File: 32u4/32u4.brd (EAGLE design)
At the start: 35.6 x 29.8 mm, 16 parts, among them J1 AVR_SPI_PRG_62X3_LOCK

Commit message: Latest controller revision
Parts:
- removed LED1: (no value), SparkFun-LED:LED-1206
- removed R5: (no value), SparkFun-Resistors:0805
- added C4: 1uF, SparkFun-Capacitors:0805
- added C5, C6: 100uF, resistor:C1608
- added JP2: (no value), pinhead:2X07
- added R6, R7: 150, SparkFun-Resistors:0805
- added R8: 330, SparkFun-Resistors:0805
- added S1: SWITCH-MOMENTARY-2SMD-3, SparkFun-Electromechanical:TACTILE_SWITCH_SMD-3
- added U$5: LED-RGB, IntegerLabs:LED-LITEON-SMD-RGB
- added U$6: TACT-SWITCHBOURNS-7914J, IntegerLabs:BOURNS-7914J
- C2, C3: value (none) -> 18pF
- D1: value (none) -> b340b; device adafruit:SMADIODE -> SparkFun-DiscreteSemi:SMB-DIODE
- J1: value AVR_SPI_PRG_62X3_LOCK -> AVR_SPI_PRG_6PTH; device SparkFun-Connectors:2X3_LOCK -> SparkFun-Connectors:2X3
- R1, R2: value (none) -> 2k
- U$4: value USB-MICRO-AB -> USBFCI-MICROB; device IntegerLabs:MOLEX-MICROAB -> IntegerLabs:USB-MICROB-FCI
- moved U$1 20.1 mm to (27.0, 3.17), turned to 180 degrees
- moved R2 12.3 mm to (5.08, 8.26), turned to 0 degrees
- moved U$4 11.4 mm to (10.2, 1.45)
- moved D1 8.47 mm to (19.1, 3.17), turned to 180 degrees
- moved R4 7.84 mm to (7.94, 7.30), turned to 90 degrees
- moved C2 7.81 mm to (23.2, 17.8), turned to 90 degrees
- moved R3 5.02 mm to (9.84, 7.30), turned to 90 degrees
- moved Y1 4.80 mm to (20.3, 16.2)
- moved C3 4.32 mm to (23.2, 14.6), turned to 270 degrees
- moved C1 4.24 mm to (11.7, 7.30), turned to 270 degrees
- moved J1 2.96 mm to (23.2, 10.2), turned to 180 degrees
- moved R1 2.29 mm to (5.08, 10.2), turned to 0 degrees
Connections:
- removed net LED: R5.2, U$2.32
- removed net N$3: LED1.A, R5.1
- new net A0: JP2.7, U$2.36
- new net A1: JP2.8, U$2.37
- new net A2: JP2.5, U$2.38
- new net A3: JP2.6, U$2.39
- new net A4: JP2.3, U$2.40
- new net A5: JP2.4, U$2.41
- new net B: R6.1, U$2.32
- new net D5: JP2.10, U$2.31
- new net D6: JP2.12, U$2.27
- new net D8: JP2.14, U$2.28
- new net D9: JP2.13, U$2.29
- new net G: R7.1, U$2.12
- new net N$10: R6.2, U$5.1
- new net N$6: R8.2, U$5.2
- new net N$7: R7.2, U$5.3
- new net R: R8.1, U$2.30
- new net SWITCH: U$2.20, U$6.POS$1
- net D+: now also U$4.P3; no longer U$4.3
- net D-: now also U$4.P2; no longer U$4.2
- net GND: now also C4.2, C5.2, C6.2, JP2.1, S1.1, U$3.BUS0, U$4.P5, U$6.NEG$1; no longer LED1.C, U$3.GND, U$4.5
- net MISO: no longer U$3.MISO
- net RESET: now also S1.4; no longer U$3.RESET
- net SCL: now also JP2.11, U$3.BUS3; no longer U$3.SCL
- net SDA: now also JP2.9, U$3.BUS1; no longer U$3.SDA
- net VBUS: now also U$4.P1; no longer U$4.1
- net VCC: now also C4.1, C5.1, C6.1, JP2.2, U$3.BUS2, U$5.4; no longer U$3.VCC
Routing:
- net GND: track 23.4 -> 132.2 mm, vias 9 -> 7
- net VCC: track 63.4 -> 97.1 mm, vias 2 -> 3
- net SCL: track 15.8 -> 48.2 mm, vias 2 -> 5
- net G: track 0.00 -> 31.4 mm
- net A4: track 0.00 -> 29.8 mm, vias 0 -> 1
- net A2: track 0.00 -> 29.2 mm, vias 0 -> 1
- net A0: track 0.00 -> 29.0 mm, vias 0 -> 1
- net MISO: track 39.7 -> 11.1 mm, vias 2 -> 1
- net A3: track 0.00 -> 28.2 mm, vias 0 -> 2
- net A5: track 0.00 -> 26.8 mm, vias 0 -> 1
- net A1: track 0.00 -> 26.0 mm, vias 0 -> 1
- net D5: track 0.00 -> 25.8 mm, vias 0 -> 1
- net D8: track 0.00 -> 24.0 mm, vias 0 -> 1
- net D9: track 0.00 -> 23.3 mm, vias 0 -> 1
- net D6: track 0.00 -> 23.1 mm, vias 0 -> 1
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- removed copper zone on layer 16, net GND
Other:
- outline, holes or cut-outs redrawn
- board text added: "+"
- board text added: "-"
- board text added: "2014-09-14"
- board text added: "A0"
- board text added: "A1"
- board text added: "A2"
- board text added: "A3"
- board text added: "A4"
- board text added: "A5"
- board text added: "Controller"
- board text added: "D5"
- board text added: "D6"
- board text added: "D8"
- board text added: "D9"
- board text added: "Integer Labs"
- board text added: "Modulo"
- board text added: "icsp"
- board text added: "reset"
- board text added: "scl"
- board text added: "sda"

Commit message: Latest version of schematics and boards
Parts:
- removed C5: 100uF, resistor:C1608
- added F2: .5A, IntegerLabs:1812
- added Q1, Q3: IRLML5203, transistor-power:MICRO3
- added Q2: DMMT5401, IntegerLabs:SOT-26
- added R5, R9: 47k 1%, SparkFun-Passives:0805
- F1: value FUSE -> 1.5A
- renumbered U$1 to F1
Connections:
- new net N$11: F2.P$2, Q1.3, Q2.6, Q3.3
- new net N$13: Q2.5, Q3.2
- new net N$14: Q2.1, Q2.2, Q2.3, R5.2
- new net N$16: Q2.4, Q3.1, R9.2
- new net N$3: F1.P$1, F2.P$1, U$4.P1
- net GND: now also R5.1, R9.1; no longer C5.2
- net N$5: now also Q1.2; no longer D1.C
- net VBUS: no longer U$4.P1
- net VCC: no longer C5.1, C6.1, F1.P$1
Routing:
- net VCC: track 97.1 -> 91.4 mm
- net N$5: track 3.20 -> 0.00 mm
- net GND: track 132.2 -> 129.0 mm
- net VBUS: track 28.6 -> 27.0 mm
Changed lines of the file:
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@@
 <attribute name="VALUE" x="4.953" y="7.112" size="0.4064" layer="27" ratio="10"/>
 </element>
-<element name="U$1" library="IntegerLabs" package="1812" value="FUSE" x="26.9875" y="3.175" rot="R180"/>
+<element name="F1" library="IntegerLabs" package="1812" value="1.5A" x="26.9875" y="3.175" rot="R180"/>
 <element name="S1" library="SparkFun-Electromechanical" package="TACTILE_SWITCH_SMD-3" value="SWITCH-MOMENTARY-2SMD-3" x="23.0505" y="27.3685" rot="R180"/>
 <element name="JP2" library="pinhead" package="2X07" value="" x="29.21" y="13.97" smashed="yes" rot="R90">
@@
 <attribute name="NAME" x="6.5405" y="12.2555" size="0.4064" layer="25" ratio="10"/>
 <attribute name="VALUE" x="6.604" y="11.6205" size="0.4064" layer="27" ratio="10"/>
-</element>
-<element name="C5" library="resistor" package="C1608" value="100uF" x="14.605" y="10.16" smashed="yes" rot="R180">
-<attribute name="NAME" x="15.367" y="9.398" size="0.508" layer="25" rot="R180"/>
-<attribute name="VALUE" x="15.875" y="11.43" size="0.508" layer="27" rot="R180"/>
 </element>
 <element name="C6" library="resistor" package="C1608" value="100uF" x="14.605" y="6.985" smashed="yes" rot="R180">
@@
 </element>
 <element name="U$6" library="IntegerLabs" package="BOURNS-7914J" value="TACT-SWITCHBOURNS-7914J" x="20.955" y="21.9075" rot="R90"/>
+<element name="Q1" library="transistor-power" package="MICRO3" value="IRLML5203" x="1.27" y="-5.08"/>
+<element name="F2" library="IntegerLabs" package="1812" value=".5A" x="2.54" y="-11.43"/>
+<element name="Q2" library="IntegerLabs" package="SOT-26" value="DMMT5401" x="-3.81" y="-11.43"/>
+<element name="R5" library="SparkFun-Passives" package="0805" value="47k 1%" x="-7.62" y="-11.43"/>
+<element name="R9" library="SparkFun-Passives" package="0805" value="47k 1%" x="-11.43" y="-11.43"/>
+<element name="Q3" library="transistor-power" package="MICRO3" value="IRLML5203" x="-10.16" y="-17.78"/>
 </elements>
 <signals>
@@
 <contactref element="S1" pad="1"/>
 <contactref element="C4" pad="2"/>
-<contactref element="C5" pad="2"/>
 <contactref element="C6" pad="2"/>
 <wire x1="5.98" y1="12.065" x2="5.98" y2="13.07" width="0.254" layer="1"/>
@@
 <wire x1="3.4925" y1="11.43" x2="5.08" y2="11.43" width="0.508" layer="16"/>
 <wire x1="5.08" y1="11.43" x2="5.08" y2="13.97" width="0.1524" layer="16"/>
-<wire x1="13.755" y1="10.16" x2="13.755" y2="6.985" width="0.508" layer="1"/>
 <wire x1="13.755" y1="6.985" x2="13.755" y2="5.6125" width="0.508" layer="1"/>
 <wire x1="13.755" y1="5.6125" x2="13.97" y2="5.3975" width="0.508" layer="1"/>
+<contactref element="R5" pad="1"/>
+<contactref element="R9" pad="1"/>
+<wire x1="-8.52" y1="-11.43" x2="-12.33" y2="-11.43" width="0" layer="19" extent="1-1"/>
+<wire x1="3.4925" y1="5.3975" x2="-8.52" y2="-11.43" width="0" layer="19" extent="1-16"/>
 </signal>
 <signal name="VCC">
@@
 <contactref element="R2" pad="1"/>
 <contactref element="R1" pad="1"/>
-<contactref element="U$1" pad="P$1"/>
 <wire x1="7.595" y1="13.885" x2="7.595" y2="15.265" width="0.1524" layer="1"/>
 <wire x1="7.595" y1="15.265" x2="6.985" y2="15.875" width="0.1524" layer="1"/>
@@
 <contactref element="JP2" pad="2"/>
 <contactref element="C4" pad="1"/>
-<contactref element="C5" pad="1"/>
-<contactref element="C6" pad="1"/>
 <wire x1="4.18" y1="12.065" x2="4.18" y2="12.0125" width="0.254" layer="1"/>
 <wire x1="4.18" y1="12.0125" x2="5.08" y2="11.1125" width="0.254" layer="1"/>
@@
 <wire x1="4.18" y1="10.16" x2="4.18" y2="10.2125" width="0.254" layer="1"/>
 <wire x1="4.18" y1="10.2125" x2="5.08" y2="11.1125" width="0.254" layer="1"/>
-<wire x1="29.5275" y1="3.175" x2="28.575" y2="3.175" width="0.254" layer="1"/>
 <wire x1="28.575" y1="3.175" x2="27.94" y2="3.81" width="0.254" layer="1"/>
 <wire x1="27.94" y1="3.81" x2="27.94" y2="6.35" width="0.254" layer="1"/>
@@
 <wire x1="16.1925" y1="5.3975" x2="15.5575" y2="6.0325" width="0.254" layer="1"/>
 <wire x1="15.5575" y1="6.0325" x2="15.5575" y2="6.8825" width="0.254" layer="1"/>
-<wire x1="15.5575" y1="6.8825" x2="15.455" y2="6.985" width="0.254" layer="1"/>
 <contactref element="J1" pad="2"/>
 <wire x1="4.995" y1="23.685" x2="3.0475" y2="23.685" width="0.1524" layer="1"/>
@@
 <wire x1="14.605" y1="15.5575" x2="14.605" y2="17.145" width="0.1524" layer="1"/>
 <wire x1="14.2875" y1="26.9875" x2="13.97" y2="26.67" width="0.1524" layer="1"/>
-<wire x1="15.455" y1="6.985" x2="15.455" y2="10.16" width="0.508" layer="1"/>
-<wire x1="15.455" y1="10.16" x2="15.455" y2="11.5325" width="0.508" layer="1"/>
 <wire x1="15.455" y1="11.5325" x2="15.24" y2="11.7475" width="0.508" layer="1"/>
 <wire x1="15.24" y1="11.7475" x2="11.7475" y2="11.7475" width="0.508" layer="1"/>
@@
 <wire x1="9.525" y1="9.2075" x2="10.16" y2="9.8425" width="0.1524" layer="16"/>
 <wire x1="10.16" y1="9.8425" x2="10.16" y2="11.43" width="0.1524" layer="16"/>
+<wire x1="15.455" y1="11.5325" x2="15.5575" y2="6.8825" width="0" layer="19" extent="1-1"/>
 </signal>
 <signal name="D-">
@@
 <signal name="VBUS">
 <contactref element="U$2" pad="7"/>
-<contactref element="U$4" pad="P1"/>
 <contactref element="D1" pad="A"/>
-<wire x1="8.86" y1="4.1478" x2="8.86" y2="3.205" width="0.254" layer="1"/>
 <wire x1="8.86" y1="3.205" x2="9.2075" y2="2.8575" width="0.254" layer="1"/>
-<wire x1="8.86" y1="4.1478" x2="8.86" y2="4.7925" width="0.254" layer="1"/>
 <wire x1="8.86" y1="4.7925" x2="8.255" y2="5.3975" width="0.254" layer="1"/>
 <wire x1="8.255" y1="5.3975" x2="6.985" y2="5.3975" width="0.254" layer="1"/>
@@
 <wire x1="11.43" y1="12.7" x2="11.43" y2="13.72" width="0.254" layer="1"/>
 <wire x1="11.43" y1="13.72" x2="11.595" y2="13.885" width="0.254" layer="1"/>
+<wire x1="8.86" y1="3.205" x2="8.86" y2="4.7925" width="0" layer="19" extent="1-1"/>
 </signal>
 <signal name="RESET">
@@
 <wire x1="20.9575" y1="13.705" x2="20.32" y2="14.3425" width="0.1524" layer="1"/>
 </signal>
-<signal name="N$5">
-<contactref element="D1" pad="C"/>
-<contactref element="U$1" pad="P$2"/>
-<wire x1="21.25" y1="3.175" x2="24.4475" y2="3.175" width="0.254" layer="1"/>
-</signal>
 <signal name="A0">
 <contactref element="U$2" pad="36"/>
@@
 <wire x1="10.4775" y1="23.1775" x2="8.89" y2="23.1775" width="0.2032" layer="1"/>
 </signal>
+<signal name="N$3">
+<contactref element="U$4" pad="P1"/>
+<contactref element="F2" pad="P$1"/>
+<contactref element="F1" pad="P$1"/>
+<wire x1="8.86" y1="4.1478" x2="29.5275" y2="3.175" width="0" layer="19" extent="1-1"/>
+<wire x1="0" y1="-11.43" x2="8.86" y2="4.1478" width="0" layer="19" extent="1-1"/>
+</signal>
+<signal name="N$5">
+<contactref element="Q1" pad="2"/>
+<contactref element="F1" pad="P$2"/>
+<wire x1="2.22" y1="-6.08" x2="24.4475" y2="3.175" width="0" layer="19" extent="1-1"/>
+</signal>
+<signal name="N$11">
+<contactref element="Q1" pad="3"/>
+<contactref element="F2" pad="P$2"/>
+<contactref element="Q2" pad="6"/>
+<contactref element="Q3" pad="3"/>
+<wire x1="-4.76" y1="-10.23" x2="-10.16" y2="-16.78" width="0" layer="19" extent="1-1"/>
+<wire x1="1.27" y1="-4.08" x2="-4.76" y2="-10.23" width="0" layer="19" extent="1-1"/>
+<wire x1="5.08" y1="-11.43" x2="1.27" y2="-4.08" width="0" layer="19" extent="1-1"/>
+</signal>
+<signal name="N$13">
+<contactref element="Q2" pad="5"/>
+<contactref element="Q3" pad="2"/>
+<wire x1="-3.81" y1="-10.23" x2="-9.21" y2="-18.78" width="0" layer="19" extent="1-1"/>
+</signal>
+<signal name="N$14">
+<contactref element="Q2" pad="2"/>
+<contactref element="Q2" pad="1"/>
+<contactref element="Q2" pad="3"/>
+<contactref element="R5" pad="2"/>
+<wire x1="-4.76" y1="-12.63" x2="-6.72" y2="-11.43" width="0" layer="19" extent="1-1"/>
+<wire x1="-3.81" y1="-12.63" x2="-4.76" y2="-12.63" width="0" layer="19" extent="1-1"/>
+<wire x1="-2.86" y1="-12.63" x2="-3.81" y2="-12.63" width="0" layer="19" extent="1-1"/>
+</signal>
+<signal name="N$16">
+<contactref element="Q2" pad="4"/>
+<contactref element="R9" pad="2"/>
+<contactref element="Q3" pad="1"/>
+<wire x1="-10.53" y1="-11.43" x2="-11.11" y2="-18.78" width="0" layer="19" extent="1-1"/>
+<wire x1="-2.86" y1="-10.23" x2="-10.53" y2="-11.43" width="0" layer="19" extent="1-1"/>
+</signal>
 </signals>

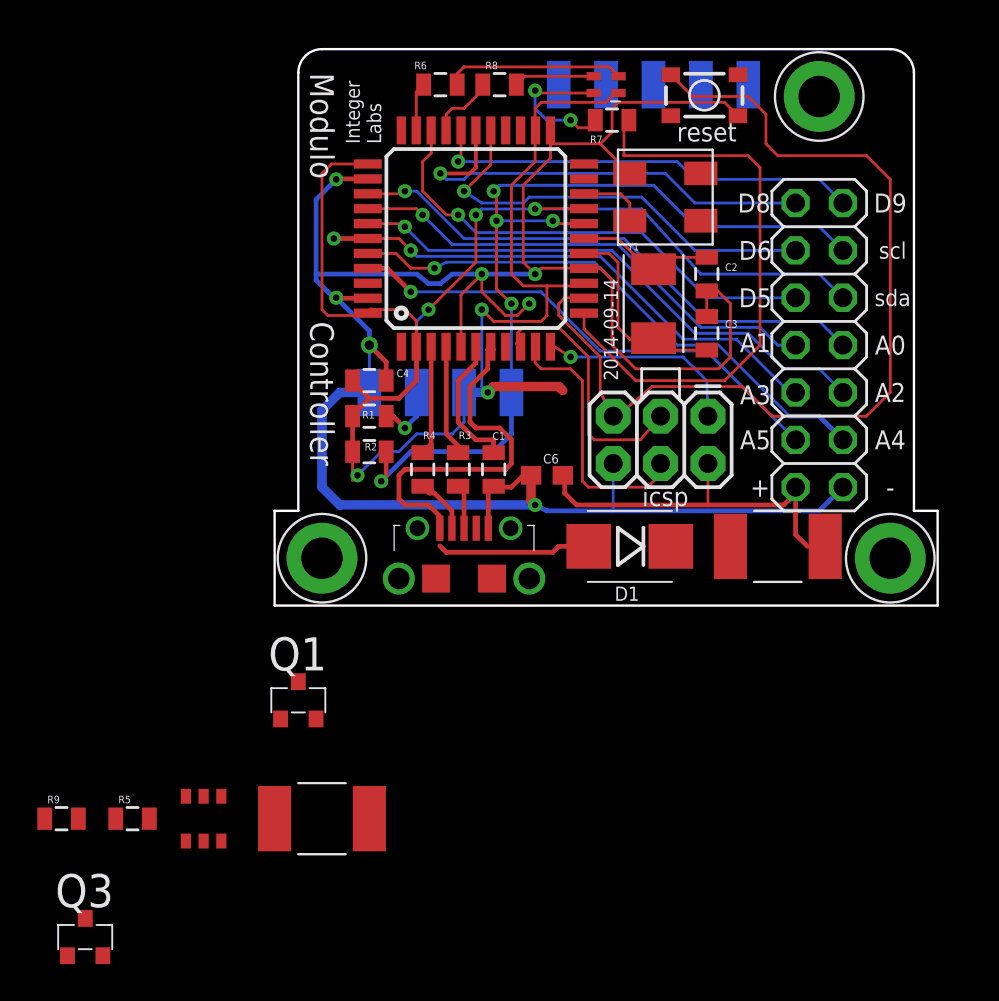
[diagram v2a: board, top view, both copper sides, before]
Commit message: New 32u4 controller board with servo pin compatible gpio and RPi reverse current protection.
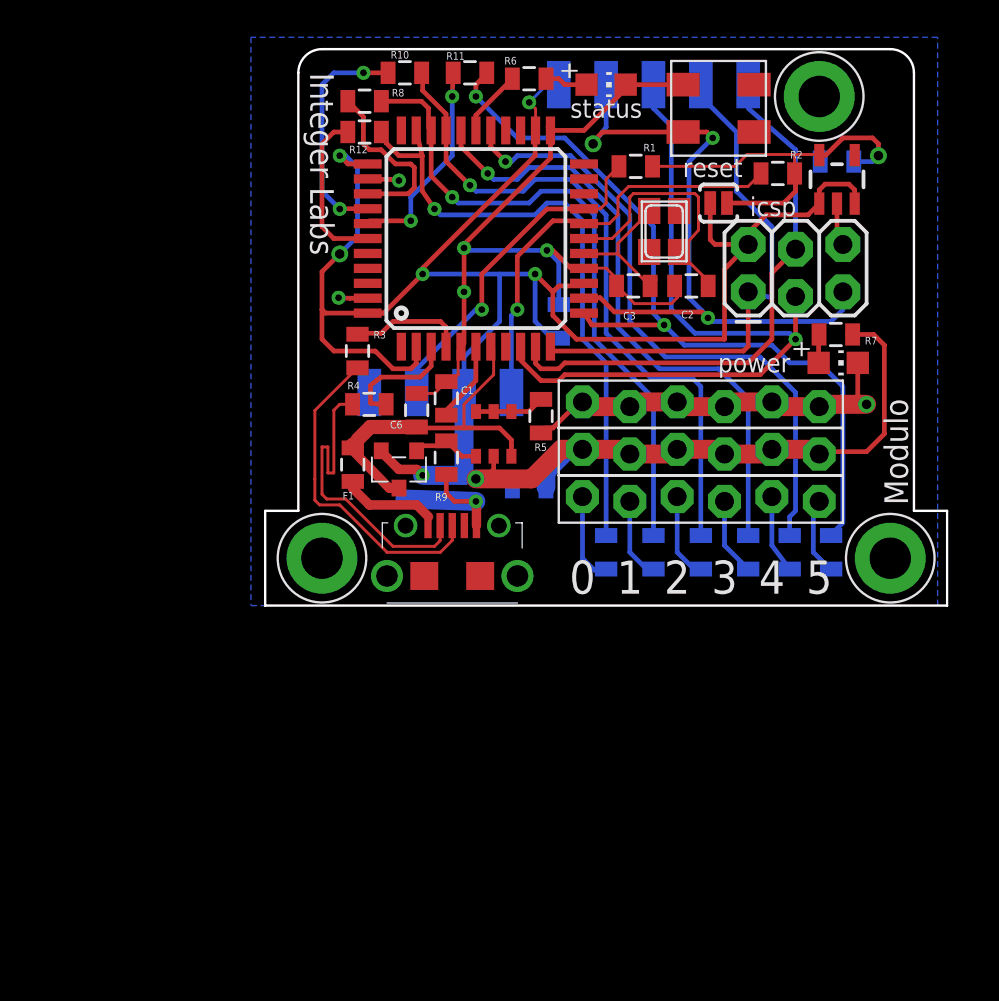
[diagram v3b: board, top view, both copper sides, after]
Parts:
- removed D1: b340b, SparkFun-DiscreteSemi:SMB-DIODE
- removed F2: .5A, IntegerLabs:1812
- removed S1: SWITCH-MOMENTARY-2SMD-3, SparkFun-Electromechanical:TACTILE_SWITCH_SMD-3
- removed U$5: LED-RGB, IntegerLabs:LED-LITEON-SMD-RGB
- removed Y1: (no value), SparkFun-FreqCtrl:CRYSTAL-TXC-7A
- added C5: 47uF, SparkFun-Capacitors:0805
- added C7: .47uF, SparkFun-Capacitors:0805
- added JP1, JP3: (no value), adafruit:1X06-BIGLOCK
- added LED1, LED2: (no value), adafruit:CHIP-LED0805
- added R10, R11, R12: 2k, SparkFun-Resistors:0805
- added R13, R14, R15, R16, R17, R18: 220, SparkFun-Resistors:0805
- added SJ1: SOLDERJUMPERNO, SparkFun-Passives:SJ_2S-NO
- added U$1: 3.3V/150mA, SparkFun-PowerIC:SOT23-5
- C4: value 1uF -> .47uF
- C6: value 100uF -> .47uF; device resistor:C1608 -> SparkFun-Capacitors:0805
- F1: value 1.5A -> MF-PSMF110X-2; device IntegerLabs:1812 -> SparkFun-Resistors:0805
- FOOTPRINT: value FOOTPRINTFOOTPRINT-2 -> Controller
- J1: value AVR_SPI_PRG_6PTH -> AVR_SPI_PRG_62X3_LOCK; device SparkFun-Connectors:2X3 -> SparkFun-Connectors:2X3_LOCK
- JP2: device pinhead:2X07 -> adafruit:1X06-BIGLOCK
- Q1: value IRLML5203 -> 16Mhz; device transistor-power:MICRO3 -> adafruit:NX3225
- Q3: value IRLML5203 -> DMG2305UX
- R5: value 47k 1% -> 10k 1%
- R6, R7: value 150 -> 680
- R8: value 330 -> 2k
- moved Q1 31.9 mm to (20.9, 20.1), turned to 90 degrees
- moved R5 30.8 mm to (14.3, 10.2), turned to 90 degrees
- moved Q3 30.2 mm to (6.67, 7.30), turned to 180 degrees
- moved R9 28.3 mm to (9.21, 7.94), turned to 90 degrees
- moved R2 26.5 mm to (27.0, 23.2), turned to 180 degrees
- moved Q2 25.8 mm to (11.7, 9.21), turned to 180 degrees
- moved F1 23.2 mm to (4.19, 7.56), turned to 90 degrees
- moved R1 19.6 mm to (19.4, 23.6), turned to 180 degrees
- moved R7 16.6 mm to (30.1, 14.5)
- moved C4 10.6 mm to (15.2, 15.2), flipped to the bottom, turned to 90 degrees
- moved R3 8.33 mm to (4.45, 13.7)
- moved C6 7.81 mm to (7.62, 10.5), turned to 90 degrees
- moved R8 7.29 mm to (4.83, 27.1)
- moved JP2 7.10 mm to (22.9, 10.8), turned to 0 degrees
- moved J1 7.01 mm to (25.4, 16.8), turned to 0 degrees
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- renumbered U$3 to FOOTPRINT
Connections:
- removed net A0: JP2.7, U$2.36
- removed net A1: JP2.8, U$2.37
- removed net A2: JP2.5, U$2.38
- removed net A3: JP2.6, U$2.39
- removed net A4: JP2.3, U$2.40
- removed net A5: JP2.4, U$2.41
- removed net B: R6.1, U$2.32
- removed net D8: JP2.14, U$2.28
- removed net G: R7.1, U$2.12
- removed net R: R8.1, U$2.30
- removed net SWITCH: U$2.20, U$6.POS$1
- new net +3.3V: C7.1, R1.1, R2.1, SJ1.2, U$1.5
- new net D10: R10.2, R16.1, U$2.30
- new net D11: R11.2, R13.1, U$2.12
- new net D13: R12.2, R18.1, U$2.32
- new net G1: Q1.4
- new net G2: Q1.2
- new net LED: R6.1, U$2.28
- new net N$12: LED2.A, R7.2
- new net N$15: C2.1, Q1.1, U$2.17
- new net N$17: JP1.3, R15.2
- new net N$18: JP1.4, R16.2
- new net N$19: JP1.5, R17.2
- new net N$20: JP1.6, R18.2
- net D5: now also R17.1, R8.2; no longer JP2.10
- net D6: now also R14.1; no longer JP2.12
- net D9: now also R15.1; no longer JP2.13
- net GND: now also C2.2, C3.2, C5.2, C7.2, JP2.2, JP2.3, JP2.4, JP2.5, JP2.6, LED1.C, LED2.C, U$1.2; no longer C2.1, C3.1, S1.1
- net MISO: now also FOOTPRINT.PROG3
- net MOSI: now also FOOTPRINT.PROG4
- net N$10: now also R10.1, U$2.37; no longer R6.2, U$5.1
- net N$11: now also R8.1, U$2.36; no longer F2.P$2, Q1.3, Q2.6, Q3.3
- net N$13: now also JP1.2, R14.2; no longer Q2.5, Q3.2
- net N$2: now also JP1.1, R13.2; no longer C2.2, U$2.17, Y1.P$2
- net N$3: now also F1.1; no longer F1.P$1, F2.P$1
- net N$4: now also C3.1, Q1.3; no longer C3.2, Y1.P$1
- net N$5: now also LED1.A, R6.2; no longer F1.P$2, Q1.2
- net N$6: now also R12.1, U$2.39; no longer R8.2, U$5.2
- net N$7: now also R11.1, U$2.38; no longer R7.2, U$5.3
- net RESET: now also FOOTPRINT.PROG1, U$6.POS$1; no longer S1.4
- net SCK: now also FOOTPRINT.PROG2
- net SCL: no longer JP2.11
- net SDA: no longer JP2.9
- net VBUS: now also C6.1, F1.2, Q2.6, Q3.3; no longer D1.A
- net VCC: now also C5.1, FOOTPRINT.PROG0, JP3.1, JP3.2, JP3.3, JP3.4, JP3.5, JP3.6, Q2.5, Q3.2, R7.1, SJ1.1, U$1.1, U$1.3; no longer JP2.2, R1.1, R2.1, U$5.4
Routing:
- net GND: track 129.0 -> 80.4 mm
- net VCC: track 91.4 -> 136.6 mm, vias 3 -> 7
- net D11: track 0.00 -> 43.3 mm, vias 0 -> 2
- net D10: track 0.00 -> 36.2 mm, vias 0 -> 1
- net D13: track 0.00 -> 33.4 mm, vias 0 -> 1
- net G: track 31.4 -> 0.00 mm
- net A4: track 29.8 -> 0.00 mm, vias 1 -> 0
- net A2: track 29.2 -> 0.00 mm, vias 1 -> 0
- net A0: track 29.0 -> 0.00 mm, vias 1 -> 0
- net A3: track 28.2 -> 0.00 mm, vias 2 -> 0
- net A5: track 26.8 -> 0.00 mm, vias 1 -> 0
- net A1: track 26.0 -> 0.00 mm, vias 1 -> 0
- net SCL: track 48.2 -> 23.1 mm, vias 5 -> 1
- net SCK: track 14.1 -> 38.9 mm, vias 0 -> 1
- net D8: track 24.0 -> 0.00 mm, vias 1 -> 0
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- added copper zone on layer 16, net GND
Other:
- board size 35.6 x 29.8 mm -> 36.6 x 29.8 mm
- board text added: "0"
- board text added: "1"
- board text added: "2"
- board text added: "3"
- board text added: "4"
- board text added: "5"
- board text added: "power"
- board text added: "status"
- board text removed: "+"
- board text removed: "-"
- board text removed: "2014-09-14"
- board text removed: "A0"
- board text removed: "A1"
- board text removed: "A2"
- board text removed: "A3"
- board text removed: "A4"
- board text removed: "A5"
- board text removed: "Controller"
- board text removed: "D5"
- board text removed: "D6"
- board text removed: "D8"
- board text removed: "D9"
- board text removed: "Integer Labs"
- board text removed: "Modulo"
- board text removed: "scl"
- board text removed: "sda"
